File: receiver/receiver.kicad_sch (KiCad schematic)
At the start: 63 parts, among them J1 USB_B_Mini, J2 Conn_01x04_Pin, J3 Conn_01x04_Pin, SW1 SW_Push, SW2 SW_SPDT, U1 AMS1117-3.3, U2 STM32F303K8Tx, Y1 16MHz

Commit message: First stage of PCB design
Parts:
- removed C13, C16, C17, C19, C20, C21: C, Capacitor_SMD:C_0603_1608Metric_Pad1.08x0.95mm_HandSolder, symbol Device:C
- removed L3, L4, L5: L, symbol Device:L
- removed R2: 10k, Resistor_SMD:R_0603_1608Metric_Pad0.98x0.95mm_HandSolder, symbol Device:R
- removed R6, R8: 100k, Resistor_SMD:R_0603_1608Metric_Pad0.98x0.95mm_HandSolder, symbol Device:R
- removed U3: ~, symbol communication_circuit:crystal
- removed U4: ~, symbol communication_circuit:transformer
- removed U6: ~, symbol communication_circuit:LT5517
- removed U7: ~, symbol communication_circuit:LNA
- added C36, C37: 100n, Capacitor_SMD:C_0603_1608Metric_Pad1.08x0.95mm_HandSolder, symbol Device:C
- added C38: 4.7u, Capacitor_SMD:C_0603_1608Metric_Pad1.08x0.95mm_HandSolder, symbol Device:C
- added D2, D3: LED, LED_SMD:LED_0805_2012Metric_Pad1.15x1.40mm_HandSolder, symbol Device:LED
- added R11, R9: 1k, Resistor_SMD:R_0603_1608Metric_Pad0.98x0.95mm_HandSolder, symbol Device:R
- added R13, R14: 1k5, Resistor_SMD:R_0603_1608Metric_Pad0.98x0.95mm_HandSolder, symbol Device:R
- added U3: Si590, Oscillator:Oscillator_SMD_IDT_JU6-6_7.0x5.0mm_P2.54mm, symbol Communication_circuit:Si590
- added U4: HMC356, Package_DFN_QFN:QFN-16-1EP_3x3mm_P0.5mm_EP1.45x1.45mm, symbol Communication_circuit:HMC356
- added U5: LT5517, Package_DFN_QFN:QFN-16-1EP_4x4mm_P0.65mm_EP2.1x2.1mm, symbol Communication_circuit:LT5517
- added U6: MABAES0054, Transformer_SMD:Transformer_MACOM_SM-22, symbol Communication_circuit:MABAES0054
- added U7: FT232RL, Package_SO:SSOP-28_5.3x10.2mm_P0.65mm, symbol Interface_USB:FT232RL
- added U8: AMK-2-13+, Communication_circuit:6-SMD-2.54, symbol Communication_circuit:AMK-2-13+
- C30, C31, C32, C33: footprint Capacitor_SMD:C_0603_1608Metric_Pad1.08x0.95mm_HandSolder -> Capacitor_SMD:C_0805_2012Metric_Pad1.18x1.45mm_HandSolder
- L1, L2, L6, L7: footprint (none) -> Inductor_SMD:L_0603_1608Metric_Pad1.05x0.95mm_HandSolder
- R5, R7: value 100k -> 1k
- SW1: footprint (none) -> Communication_circuit:PUSH
- Y1: footprint (none) -> Crystal:Crystal_HC49-4H_Vertical
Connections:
- net +3V3: now also C37.2, U3.1 (NC), U3.6 (VDD), U7.17 (3V3OUT), U7.4 (VCCIO)
- net ADC1_IN1: now also R5.2; no longer R5.1
- net ADC1_IN2: now also R7.2
- net ADC1_IN3: now also R9.2; no longer R7.1
- net ADC1_IN4: now also R11.2
- net BPF_output: now also C11.2, U6.4 (INPUT1)
- net EN: now also U5.5 (EN)
- net GND: now also C36.1, C37.1, C38.1, U3.3 (GND), U4.16 (GND), U4.17 (EPAD), U4.2 (GND), U4.4 (GND), U4.6 (GND), U5.1 (GND_RF), U5.11 (GND), U5.17 (GND), U5.4 (GND_RF), U5.9 (GND), U6.2 (GND), U6.5 (INPUT2), U7.18 (GND), U7.21 (GND), U7.25 (AGND), U7.7 (GND), U8.1 (GND), U8.4 (GND), U8.5 (GND)
- net LO_OUT: now also U8.6 (OUT)
- net RF_ANTENNA_INPUT: now also U4.3 (RF_IN)
- net RF_OUTPUT: now also U4.11 (RF_OUT)
- net SWCLK: now also J3.3 (Pin_3); no longer J3.2 (Pin_2)
- net SWDIO: now also J3.2 (Pin_2); no longer J3.3 (Pin_3)
- net USART1_RX: now also J2.2 (Pin_2), U7.1 (TXD); no longer J2.3 (Pin_3)
- net USART1_TX: now also J2.3 (Pin_3), U7.5 (RXD); no longer J2.2 (Pin_2)
- net USB_D+: now also U7.15 (USBD+)
- net USB_D-: now also U7.16 (USBD-)
- net at C34.1: now also U4.7 (ACG)
- net at C29.1: now also U5.10 (2XLO)
- net at C27.2: now also U5.2 (RF_P)
- net at C28.1: now also U5.3 (RF_N)
- net at C27.1: now also U6.1 (OUTPUT1)
- net at C28.2: now also U6.3 (OUTPUT2)
- net at L7.2: now also U4.15 (VDD)
- net USART1_CTS: now reaches U2.21 (PA11)
- net USART1_CTS: now also U7.3 (RTS)
- net USART1_RTS: now reaches U2.22 (PA12)
- net USART1_RTS: now also U7.11 (CTS)
- net VBUS renamed +5V
- net +5V: now also C36.2, C38.2, R13.1, R14.1, U5.12 (VCC), U5.6 (VCC), U5.7 (VCC), U5.8 (VCC), U7.20 (VCC)
- new net: U3.4 (CLK_P), U8.3 (IN)
- new net: D2.2 (A), R13.2
- new net: D3.2 (A), R14.2
- new net I_OUT_N: R7.1, U5.15 (I_OUT_N)
- new net I_OUT_P: R5.1, U5.16 (I_OUT_P)
- new net Q_OUT_N: R11.1, U5.13 (Q_OUT_N)
- new net Q_OUT_P: R9.1, U5.14 (Q_OUT_P)
- new net RX_LED: D2.1 (K), U7.22 (CBUS1)
- new net TX_LED: D3.1 (K), U7.23 (CBUS0)
- no-connect marks 25 -> 35
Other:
- note added: "https://botland.com.pl/usb-uart.html"
- note added: "https://www.tme.eu/pl/ft232rl-reel/"
- note removed: "Dodać filtr RC. Rezystory szeregowo"
- moved on the sheet: C10, C11, C12, C14, C15, C18, C2, C22, C23, C24, C25, C26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

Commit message: Finished PCB design
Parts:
- removed U3: Si590, Oscillator:Oscillator_SMD_IDT_JU6-6_7.0x5.0mm_P2.54mm, symbol Communication_circuit:Si590
- removed U8: AMK-2-13+, Communication_circuit:6-SMD-2.54, symbol Communication_circuit:AMK-2-13+
- added AE1: Antenna_Shield, Connector_Coaxial:U.FL_Molex_MCRF_73412-0110_Vertical, symbol Device:Antenna_Shield
- added C13, C16: 220p, Capacitor_SMD:C_0603_1608Metric_Pad1.08x0.95mm_HandSolder, symbol Device:C
- added H1, H2, H3, H4: MountingHole_Pad, MountingHole:MountingHole_2.2mm_M2_DIN965_Pad, symbol Mechanical:MountingHole_Pad
- added R2: 1.5k, Resistor_SMD:R_0603_1608Metric_Pad0.98x0.95mm_HandSolder, symbol Device:R
- added R6: 3.9k, Resistor_SMD:R_0603_1608Metric_Pad0.98x0.95mm_HandSolder, symbol Device:R
- added RV1: R_Potentiometer, Potentiometer_SMD:Potentiometer_ACP_CA6-VSMD_Vertical, symbol Device:R_Potentiometer
- added U3: MAX2622, Package_SO:TSSOP-8_4.4x3mm_P0.65mm, symbol Communication_circuit:MAX2622
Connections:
- net +3V3: now also R13.1, R14.1, C13.1, C16.1, R6.2, U3.4 (SHDN), U3.5 (VCC), U3.6 (VCC); no longer C37.2, U7.17 (3V3OUT), U7.4 (VCCIO)
- net +5V: no longer R13.1, R14.1
- net GND: now also AE1.2 (Shield), C13.2, C16.2, H1.1, H2.1, H3.1, H4.1, RV1.3, U3.3 (GND), U3.8 (GND)
- net LO_OUT: now also U3.7 (OUT)
- net SWCLK: now also J3.2 (Pin_2); no longer J3.3 (Pin_3)
- net SWDIO: now also J3.3 (Pin_3); no longer J3.2 (Pin_2)
- net USART1_RX: now also J2.3 (Pin_3); no longer J2.2 (Pin_2)
- net USART1_TX: now also J2.2 (Pin_2); no longer J2.3 (Pin_3)
- net USB_D+: now also R2.2
- net RF_ANTENNA_INPUT: no longer names the net of L6.1, U4.3 (RF_IN)
- net RF_ANTENNA_INPUT: now also AE1.1 (A)
- net USART1_CTS: no longer names the net of U7.3 (RTS)
- net USART1_CTS: no longer U2.21 (PA11)
- net USART1_RTS: no longer names the net of U7.11 (CTS)
- net USART1_RTS: no longer U2.22 (PA12)
- new net: R6.1, RV1.1
- new net: RV1.2, U3.2 (TUNE)
- new net 3V3: C37.2, R2.1, U7.17 (3V3OUT), U7.4 (VCCIO)
- no-connect marks 35 -> 37
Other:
- note added: "To sprawdzić czy footprint się zgadza"
- note removed: "Si531"
- moved on the sheet: C1, C11, C12, C15, C18, C22, C23, C24, C25, C26, C27, C28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

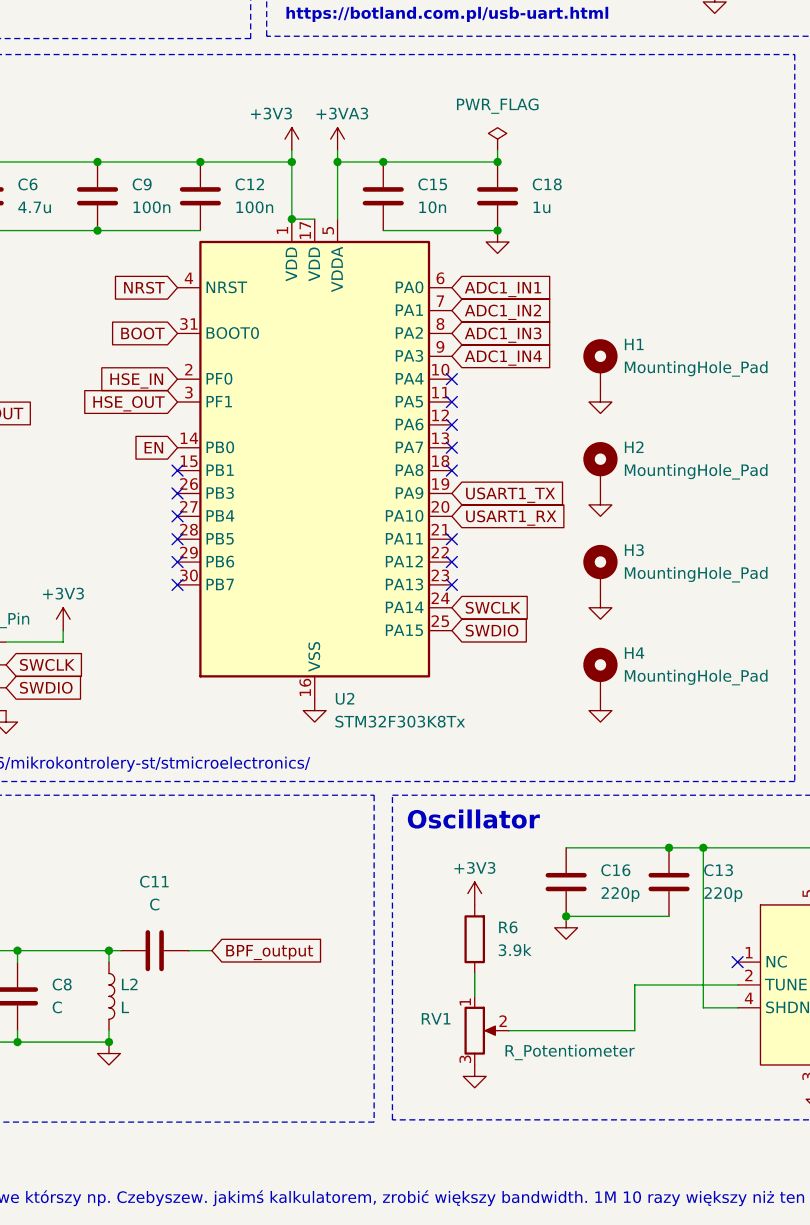
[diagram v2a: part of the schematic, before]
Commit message: First design of sended PCBs
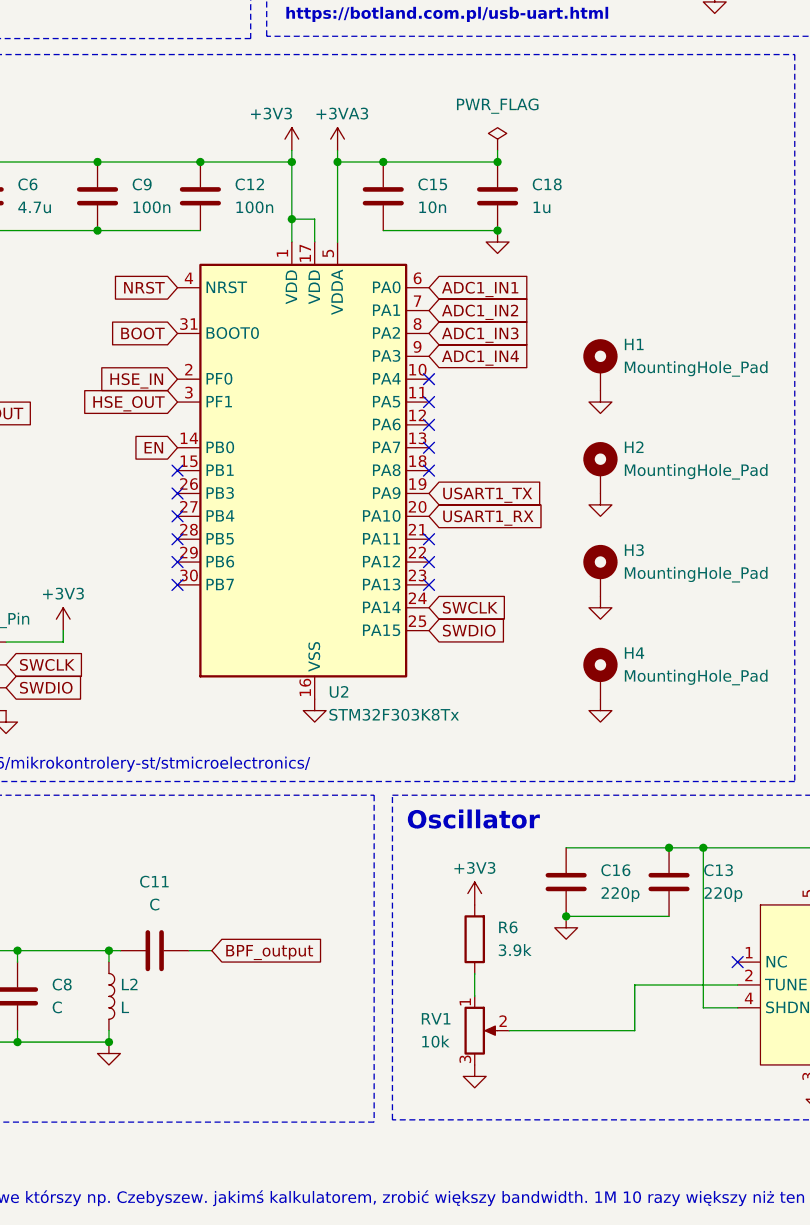
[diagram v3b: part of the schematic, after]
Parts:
- RV1: value R_Potentiometer -> 10k; footprint Potentiometer_SMD:Potentiometer_ACP_CA6-VSMD_Vertical -> Potentiometer_SMD:Potentiometer_Bourns_TC33X_Vertical
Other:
- moved on the sheet: U2
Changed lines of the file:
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@@
 	)
 	(junction
-		(at 92.71 96.52)
+		(at 264.16 140.97)
 		(diameter 0)
 		(color 0 0 0 0)
 	)
 	(junction
-		(at 264.16 140.97)
+		(at 243.84 69.85)
 		(diameter 0)
 		(color 0 0 0 0)
 	)
 	(junction
-		(at 243.84 69.85)
+		(at 92.71 96.52)
 		(diameter 0)
 		(color 0 0 0 0)
@@
 	)
 	(no_connect
-		(at 110.49 137.16)
+		(at 107.95 137.16)
 	)
 	(no_connect
@@
 	)
 	(no_connect
-		(at 110.49 124.46)
+		(at 107.95 124.46)
 	)
 	(no_connect
@@
 	)
 	(no_connect
-		(at 110.49 114.3)
+		(at 107.95 114.3)
 	)
 	(no_connect
@@
 	)
 	(no_connect
-		(at 110.49 121.92)
+		(at 107.95 121.92)
 	)
 	(no_connect
-		(at 110.49 116.84)
+		(at 107.95 116.84)
 	)
 	(no_connect
@@
 	)
 	(no_connect
-		(at 110.49 134.62)
+		(at 107.95 134.62)
 	)
 	(no_connect
@@
 	)
 	(no_connect
-		(at 110.49 119.38)
+		(at 107.95 119.38)
 	)
 	(no_connect
@@
 	)
 	(no_connect
-		(at 110.49 132.08)
+		(at 107.95 132.08)
 	)
 	(no_connect
@@
 	(wire
 		(pts
+			(xy 97.79 90.17) (xy 97.79 99.06)
+		)
+		(stroke
+			(width 0)
+			(type default)
+		)
+	)
+	(wire
+		(pts
 			(xy 201.93 92.71) (xy 201.93 93.98)
 		)
@@
 	(wire
 		(pts
+			(xy 95.25 96.52) (xy 95.25 99.06)
+		)
+		(stroke
+			(width 0)
+			(type default)
+		)
+	)
+	(wire
+		(pts
 			(xy 264.16 140.97) (xy 264.16 142.24)
 		)
@@
 	(wire
 		(pts
-			(xy 97.79 90.17) (xy 97.79 96.52)
-		)
-		(stroke
-			(width 0)
-			(type default)
-		)
-	)
-	(wire
-		(pts
 			(xy 176.53 92.71) (xy 189.23 92.71)
 		)
@@
 	(wire
 		(pts
+			(xy 92.71 96.52) (xy 92.71 99.06)
+		)
+		(stroke
+			(width 0)
+			(type default)
+		)
+	)
+	(wire
+		(pts
 			(xy 130.81 186.69) (xy 116.84 186.69)
 		)
@@
 	(global_label "ADC1_IN1"
 		(shape input)
-		(at 110.49 104.14 0)
+		(at 107.95 104.14 0)
 		(fields_autoplaced yes)
 		(effects
@@
 		)
 		(property "Intersheetrefs" "${INTERSHEET_REFS}"
-			(at 122.4257 104.14 0)
+			(at 119.8857 104.14 0)
 			(effects
 				(font
@@
 	(global_label "USART1_TX"
 		(shape input)
-		(at 110.49 127 0)
+		(at 107.95 127 0)
 		(fields_autoplaced yes)
 		(effects
@@
 		)
 		(property "Intersheetrefs" "${INTERSHEET_REFS}"
-			(at 123.6956 127 0)
+			(at 121.1556 127 0)
 			(effects
 				(font
@@
 	(global_label "ADC1_IN4"
 		(shape input)
-		(at 110.49 111.76 0)
+		(at 107.95 111.76 0)
 		(fields_autoplaced yes)
 		(effects
@@
 		)
 		(property "Intersheetrefs" "${INTERSHEET_REFS}"
-			(at 122.4257 111.76 0)
+			(at 119.8857 111.76 0)
 			(effects
 				(font
@@
 	(global_label "ADC1_IN3"
 		(shape input)
-		(at 110.49 109.22 0)
+		(at 107.95 109.22 0)
 		(fields_autoplaced yes)
 		(effects
@@
 		)
 		(property "Intersheetrefs" "${INTERSHEET_REFS}"
-			(at 122.4257 109.22 0)
+			(at 119.8857 109.22 0)
 			(effects
 				(font
@@
 	(global_label "USART1_RX"
 		(shape input)
-		(at 110.49 129.54 0)
+		(at 107.95 129.54 0)
 		(fields_autoplaced yes)
 		(effects
@@
 		)
 		(property "Intersheetrefs" "${INTERSHEET_REFS}"
-			(at 123.998 129.54 0)
+			(at 121.458 129.54 0)
 			(effects
 				(font
@@
 	(global_label "ADC1_IN2"
 		(shape input)
-		(at 110.49 106.68 0)
+		(at 107.95 106.68 0)
 		(fields_autoplaced yes)
 		(effects
@@
 		)
 		(property "Intersheetrefs" "${INTERSHEET_REFS}"
-			(at 122.4257 106.68 0)
+			(at 119.8857 106.68 0)
 			(effects
 				(font
@@
 	(global_label "SWDIO"
 		(shape input)
-		(at 110.49 142.24 0)
+		(at 107.95 142.24 0)
 		(fields_autoplaced yes)
 		(effects
@@
 		)
 		(property "Intersheetrefs" "${INTERSHEET_REFS}"
-			(at 119.3414 142.24 0)
+			(at 116.8014 142.24 0)
 			(effects
 				(font
@@
 	(global_label "SWCLK"
 		(shape input)
-		(at 110.49 139.7 0)
+		(at 107.95 139.7 0)
 		(fields_autoplaced yes)
 		(effects
@@
 		)
 		(property "Intersheetrefs" "${INTERSHEET_REFS}"
-			(at 119.7042 139.7 0)
+			(at 117.1642 139.7 0)
 			(effects
 				(font
@@
 			)
 		)
-		(property "Value" "R_Potentiometer"
-			(at 130.81 188.976 0)
+		(property "Value" "10k"
+			(at 110.236 187.96 0)
 			(effects
 				(font
@@
 			)
 		)
-		(property "Footprint" "Potentiometer_SMD:Potentiometer_ACP_CA6-VSMD_Vertical"
+		(property "Footprint" "Potentiometer_SMD:Potentiometer_Bourns_TC33X_Vertical"
 			(at 113.03 186.69 0)
 			(effects
@@
 		)
 		(instances
-			(project ""
+			(project "receiver"
 				(path "/9c85b918-2477-4635-b284-aa7b3f9ff354"
 					(reference "RV1")
@@
 	)
 	(symbol
-		(lib_name "STM32F303K8Tx_1")
 		(lib_id "MCU_ST_STM32F3:STM32F303K8Tx")
-		(at 95.25 124.46 0)
+		(at 92.71 124.46 0)
 		(unit 1)
 		(exclude_from_sim no)
@@
 		(on_board yes)
 		(dnp no)
-		(fields_autoplaced yes)
 		(property "Reference" "U2"
-			(at 97.4441 149.86 0)
+			(at 96.774 149.098 0)
 			(effects
 				(font
@@
 		)
 		(property "Value" "STM32F303K8Tx"
-			(at 97.4441 152.4 0)
+			(at 96.774 151.638 0)
 			(effects
 				(font
@@
 		)
 		(property "Footprint" "Package_QFP:LQFP-32_7x7mm_P0.8mm"
-			(at 82.55 147.32 0)
+			(at 80.01 147.32 0)
 			(effects
 				(font
@@
 		)
 		(property "Datasheet" "https://www.st.com/resource/en/datasheet/stm32f303k8.pdf"
-			(at 95.25 124.46 0)
+			(at 92.71 124.46 0)
 			(effects
 				(font
@@
 		)
 		(property "Description" "STMicroelectronics Arm Cortex-M4 MCU, 64KB flash, 16KB RAM, 72 MHz, 2.0-3.6V, 25 GPIO, LQFP32"
-			(at 95.25 124.46 0)
+			(at 92.71 124.46 0)
 			(effects
 				(font
